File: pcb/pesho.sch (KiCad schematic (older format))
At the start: 64 parts, among them IC1 4N25, IC2 4N25, IC3 4N25, IC4 4N25, IC5 4N25, IC6 4N25, P1 Power, P2 Bulkey, P3 Raspberry Pi CONN, P4 Serial, U1 JE-112D, U2 JE-112D, U3 JE-112D

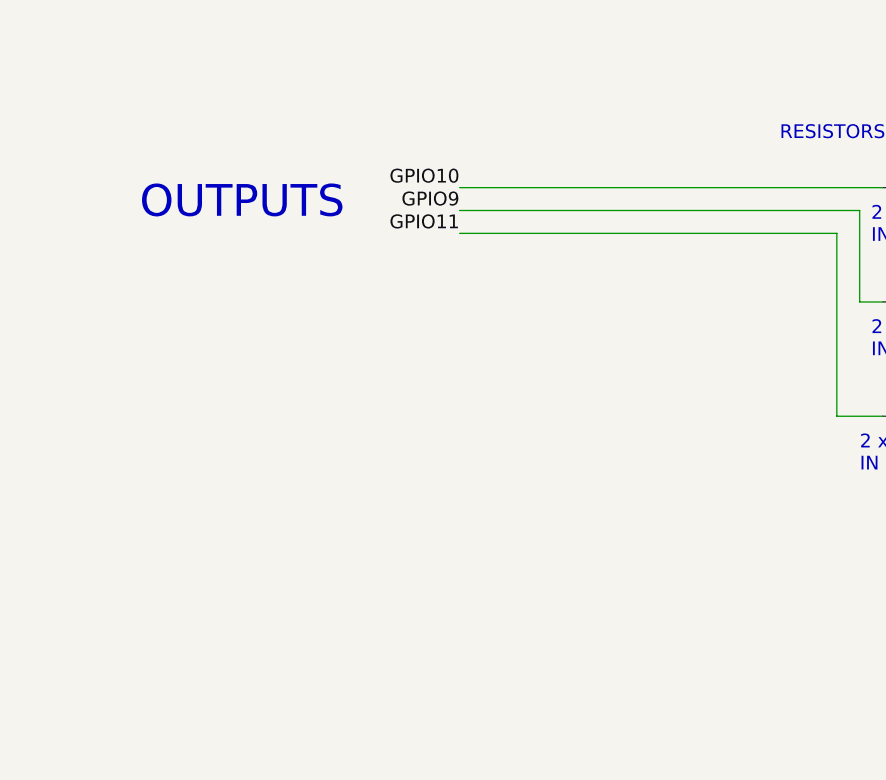
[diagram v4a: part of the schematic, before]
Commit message: Last update ! The PCB is not working, because of the relays.
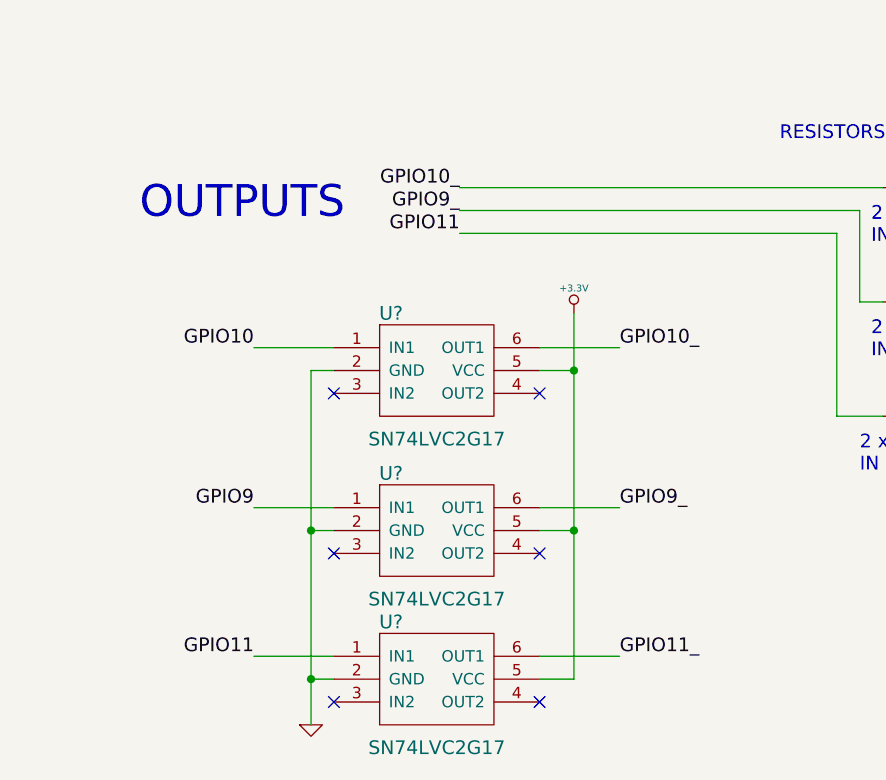
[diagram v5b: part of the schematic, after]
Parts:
- added U? (x3): SN74LVC2G17, symbol SN74LVC2G17
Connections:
- net +3.3V: now also U?.5 (VCC), U?.5 (VCC), U?.5 (VCC)
- net GND: now also U?.2 (GND), U?.2 (GND), U?.2 (GND)
- net GPIO10: now also U?.1 (IN1); no longer R4.2
- net GPIO11: now also U?.1 (IN1)
- net GPIO9: now also U?.1 (IN1); no longer R5.2
- new net GPIO10_: R4.2, U?.6 (OUT1)
- new net GPIO11_: U?.6 (OUT1)
- new net GPIO9_: R5.2, U?.6 (OUT1)
- no-connect marks 18 -> 24
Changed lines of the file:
@@
 Text Label 10750 7650 0    60   ~ 0
 UNLOCK
-Text Label 5550 6900 2    60   ~ 0
+Text Label 4650 7600 2    60   ~ 0
 GPIO10
 Text Label 5550 7000 2    60   ~ 0
-GPIO9
+GPIO9_
 Text Label 5550 7100 2    60   ~ 0
 GPIO11
@@
 	9250 2850 9250 2650
 Connection ~ 9600 2650
+$Comp
+L SN74LVC2G17 U?
+U 1 1 5470662A
+P 5450 7700
+F 0 "U?" H 5250 7950 60  0000 C CNN
+F 1 "SN74LVC2G17" H 5450 7400 60  0000 C CNN
+F 2 "" H 5450 7700 60  0000 C CNN
+F 3 "" H 5450 7700 60  0000 C CNN
+	1    5450 7700
+	1    0    0    -1
+$EndComp
+$Comp
+L SN74LVC2G17 U?
+U 1 1 54706D68
+P 5450 8400
+F 0 "U?" H 5250 8650 60  0000 C CNN
+F 1 "SN74LVC2G17" H 5450 8100 60  0000 C CNN
+F 2 "" H 5450 8400 60  0000 C CNN
+F 3 "" H 5450 8400 60  0000 C CNN
+	1    5450 8400
+	1    0    0    -1
+$EndComp
+$Comp
+L SN74LVC2G17 U?
+U 1 1 54706EA8
+P 5450 9050
+F 0 "U?" H 5250 9300 60  0000 C CNN
+F 1 "SN74LVC2G17" H 5450 8750 60  0000 C CNN
+F 2 "" H 5450 9050 60  0000 C CNN
+F 3 "" H 5450 9050 60  0000 C CNN
+	1    5450 9050
+	1    0    0    -1
+$EndComp
+Wire Wire Line
+	6050 7450 6050 9050
+Wire Wire Line
+	6050 9050 5900 9050
+Wire Wire Line
+	5900 8400 6050 8400
+Connection ~ 6050 8400
+Wire Wire Line
+	5900 7700 6050 7700
+Connection ~ 6050 7700
+$Comp
+L +3.3V #PWR?
+U 1 1 547076AD
+P 6050 7450
+F 0 "#PWR?" H 6050 7410 30  0001 C CNN
+F 1 "+3.3V" H 6050 7560 30  0000 C CNN
+F 2 "" H 6050 7450 60  0000 C CNN
+F 3 "" H 6050 7450 60  0000 C CNN
+	1    6050 7450
+	1    0    0    -1
+$EndComp
+Wire Wire Line
+	5900 7600 6250 7600
+Text Label 5550 6900 2    60   ~ 0
+GPIO10_
+Text Label 4650 8300 2    60   ~ 0
+GPIO9
+Text Label 4650 8950 2    60   ~ 0
+GPIO11
+Wire Wire Line
+	4650 8950 5000 8950
+Wire Wire Line
+	4650 8300 5000 8300
+Wire Wire Line
+	4650 7600 5000 7600
+Wire Wire Line
+	5000 7700 4900 7700
+Wire Wire Line
+	4900 7700 4900 9250
+Wire Wire Line
+	5000 8400 4900 8400
+Connection ~ 4900 8400
+Wire Wire Line
+	5000 9050 4900 9050
+Connection ~ 4900 9050
+$Comp
+L GND #PWR?
+U 1 1 5470A2ED
+P 4900 9250
+F 0 "#PWR?" H 4900 9250 30  0001 C CNN
+F 1 "GND" H 4900 9180 30  0001 C CNN
+F 2 "" H 4900 9250 60  0000 C CNN
+F 3 "" H 4900 9250 60  0000 C CNN
+	1    4900 9250
+	1    0    0    -1
+$EndComp
+Text Label 6250 7600 0    60   ~ 0
+GPIO10_
+Text Label 6250 8300 0    60   ~ 0
+GPIO9_
+Text Label 6250 8950 0    60   ~ 0
+GPIO11_
+Wire Wire Line
+	5900 8300 6250 8300
+Wire Wire Line
+	5900 8950 6250 8950
+NoConn ~ 5000 7800
+NoConn ~ 5900 7800
+NoConn ~ 5000 8500
+NoConn ~ 5900 8500
+NoConn ~ 5000 9150
+NoConn ~ 5900 9150
 $EndSCHEMATC
